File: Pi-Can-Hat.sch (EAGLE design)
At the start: 51 parts, among them IC1 MCP2515-I/SO, IC2 MCP2562-E/SN, IC3 MCP2515-I/SO, IC4 MCP2562-E/SN, IC5 MEGA8-AI, J1 RJ45 CAN.Bus, Q1 16MHz, Q2 IRF7410, Q3 16MHz, Q4 16MHz, U1 TSR 2-2450

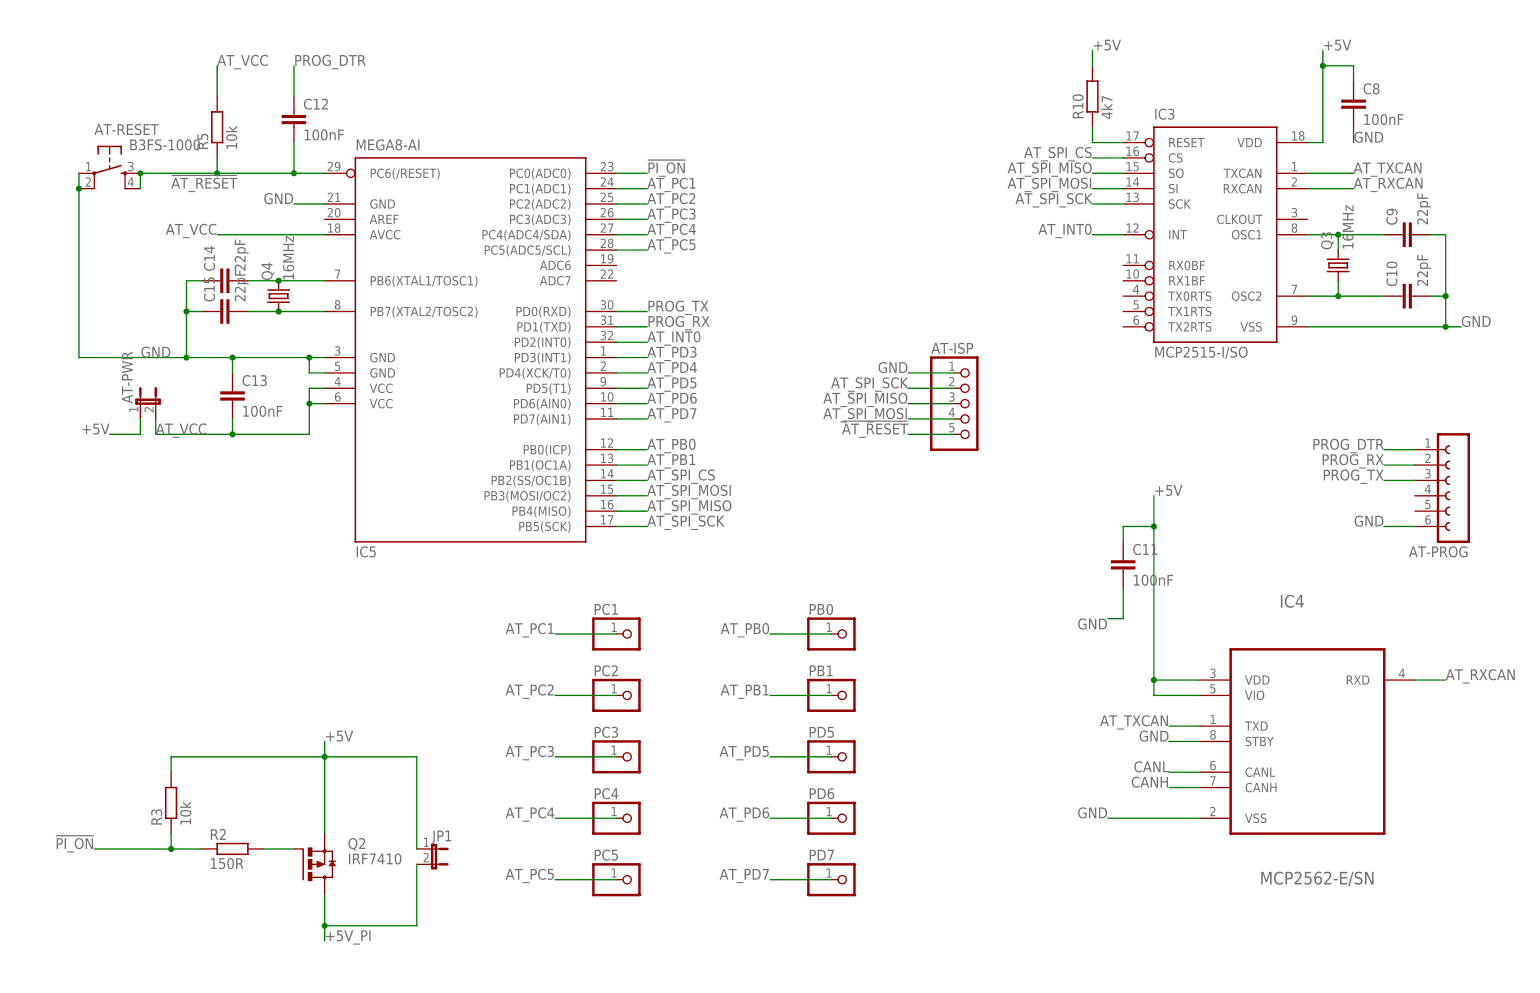
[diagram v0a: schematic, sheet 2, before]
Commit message: Zusätzliche Kondensatoren auf CAN-Hat gegen Reset beim Einschalten des Pis
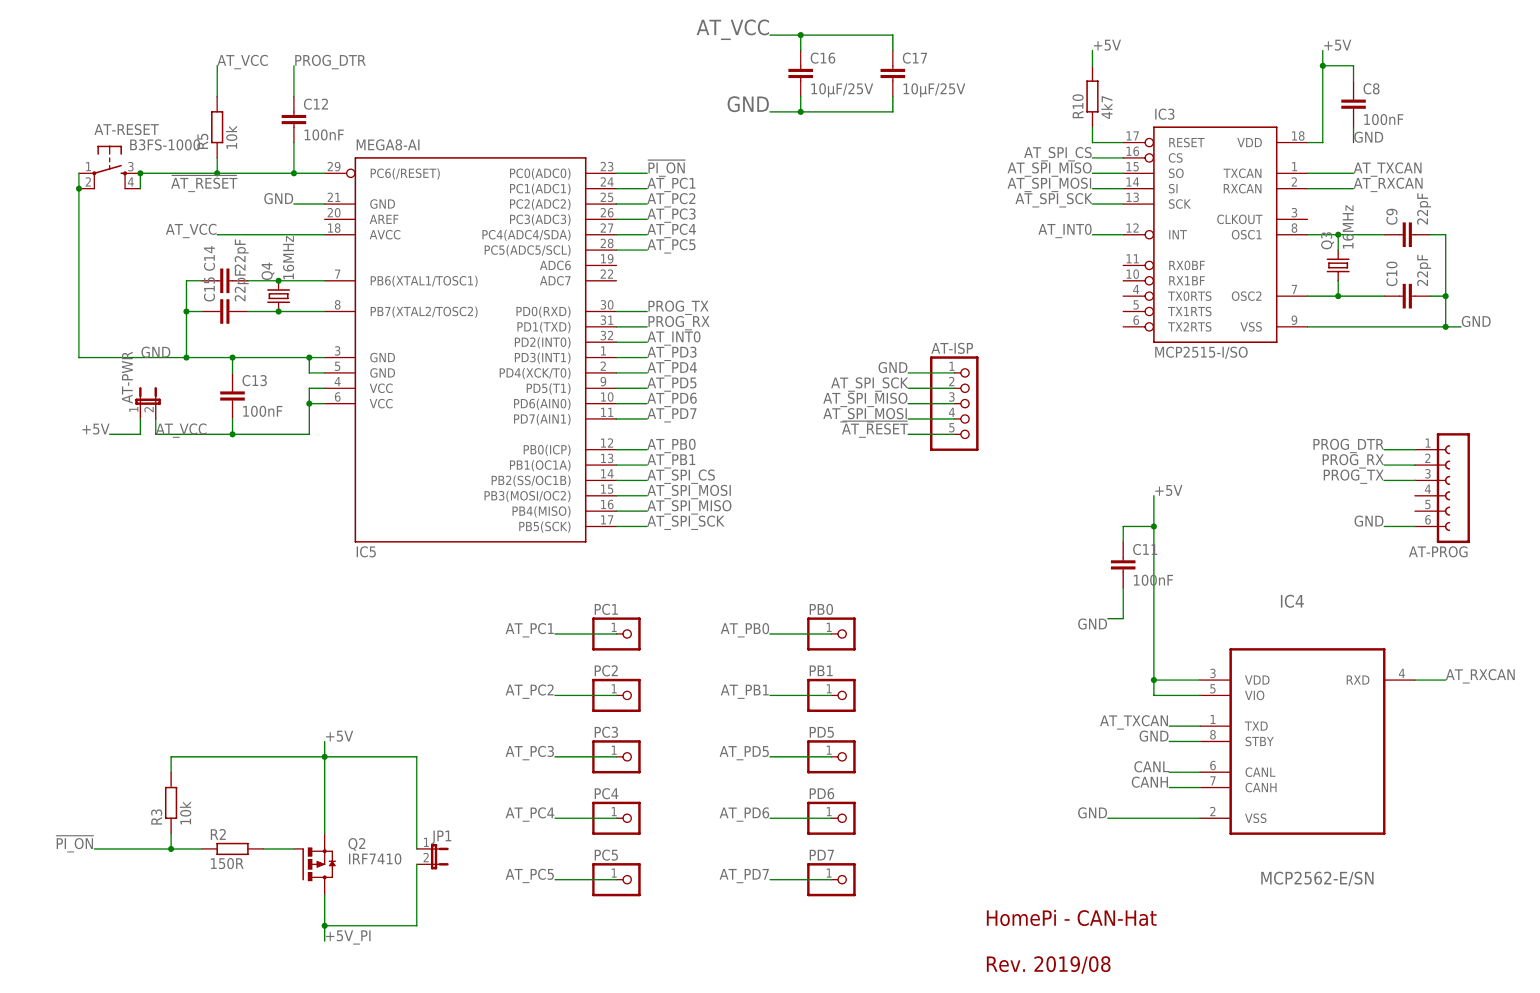
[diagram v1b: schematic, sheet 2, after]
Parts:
- added C16, C17: 10µF/25V, rcl:C-EUC1206
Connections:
- net AT_VCC: now also C16.1, C17.1
- net GND: now also C16.2, C17.2
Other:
- note added: "HomePi - CAN-Hat Rev. 2019/08"
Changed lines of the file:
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@@
 <part name="JP2" library="pinhead" deviceset="PINHD-1X2" device=""/>
 <part name="JP3" library="pinhead" deviceset="PINHD-1X2" device=""/>
+<part name="C16" library="rcl" deviceset="C-EU" device="C1206" value="10µF/25V"/>
+<part name="C17" library="rcl" deviceset="C-EU" device="C1206" value="10µF/25V"/>
 </parts>
 <sheets>
 <sheet>
 <plain>
+<text x="160.02" y="15.24" size="2.54" layer="94" align="top-left">HomePi - CAN-Hat
+Rev. 2019/08</text>
 </plain>
 <instances>
@@
 <instance part="C6" gate="G$1" x="15.24" y="149.86"/>
 <instance part="DISPLAY-POWER" gate="G$1" x="60.96" y="119.38"/>
-<instance part="U$1" gate="G$1" x="167.64" y="12.7"/>
+<instance part="U$1" gate="G$1" x="236.22" y="25.4"/>
 <instance part="JP2" gate="G$1" x="134.62" y="76.2"/>
 <instance part="JP3" gate="G$1" x="134.62" y="58.42"/>
@@
 <sheet>
 <plain>
+<text x="160.02" y="15.24" size="2.54" layer="94" align="top-left">HomePi - CAN-Hat
+Rev. 2019/08</text>
 </plain>
 <instances>
@@
 <instance part="PC3" gate="G$1" x="101.6" y="40.64"/>
 <instance part="JP1" gate="A" x="68.58" y="25.4" rot="R270"/>
+<instance part="C16" gate="G$1" x="129.54" y="154.94"/>
+<instance part="C17" gate="G$1" x="144.78" y="154.94"/>
 </instances>
 <busses>
@@
 <pinref part="AT-ISP" gate="A" pin="1"/>
 </segment>
+<segment>
+<pinref part="C17" gate="G$1" pin="2"/>
+<wire x1="144.78" y1="149.86" x2="144.78" y2="147.32" width="0.1524" layer="91"/>
+<pinref part="C16" gate="G$1" pin="2"/>
+<wire x1="144.78" y1="147.32" x2="129.54" y2="147.32" width="0.1524" layer="91"/>
+<wire x1="129.54" y1="147.32" x2="129.54" y2="149.86" width="0.1524" layer="91"/>
+<wire x1="129.54" y1="147.32" x2="124.46" y2="147.32" width="0.1524" layer="91"/>
+<junction x="129.54" y="147.32"/>
+<label x="124.46" y="147.32" size="2.54" layer="95" rot="MR0"/>
+</segment>
 </net>
 <net name="N$6" class="0">
@@
 <label x="33.02" y="154.94" size="1.778" layer="95"/>
 </segment>
+<segment>
+<pinref part="C16" gate="G$1" pin="1"/>
+<wire x1="129.54" y1="157.48" x2="129.54" y2="160.02" width="0.1524" layer="91"/>
+<pinref part="C17" gate="G$1" pin="1"/>
+<wire x1="129.54" y1="160.02" x2="144.78" y2="160.02" width="0.1524" layer="91"/>
+<wire x1="144.78" y1="160.02" x2="144.78" y2="157.48" width="0.1524" layer="91"/>
+<wire x1="129.54" y1="160.02" x2="124.46" y2="160.02" width="0.1524" layer="91"/>
+<junction x="129.54" y="160.02"/>
+<label x="124.46" y="160.02" size="2.54" layer="95" rot="MR0"/>
+</segment>
 </net>
 <net name="!PI_ON" class="0">
@@
 </schematic>
 </drawing>
+<compatibility>
+<note version="6.3" minversion="6.2.2" severity="warning">
+Since Version 6.2.2 text objects can contain more than one line,
+which will not be processed correctly with this version.
+</note>
+</compatibility>
 </eagle>
